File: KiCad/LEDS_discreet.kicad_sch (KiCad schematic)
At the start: 2 parts, among them U107 74HC595D,118

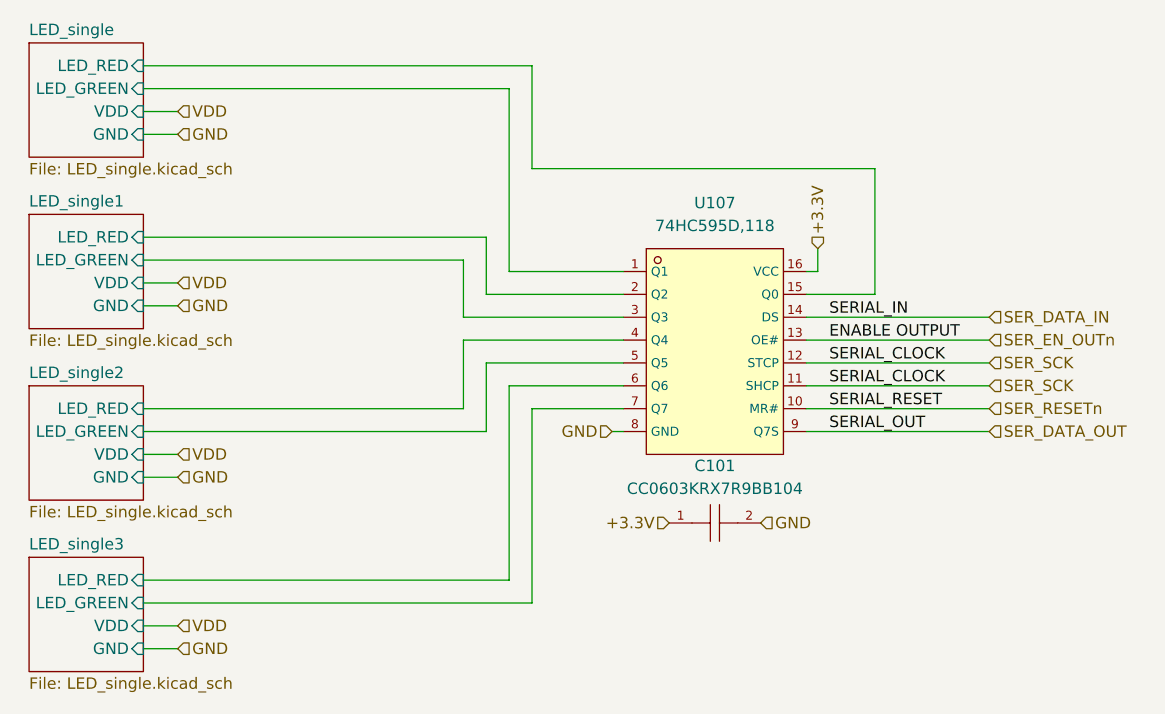
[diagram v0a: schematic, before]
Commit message: Ready for PCB layout with discreet LEDs
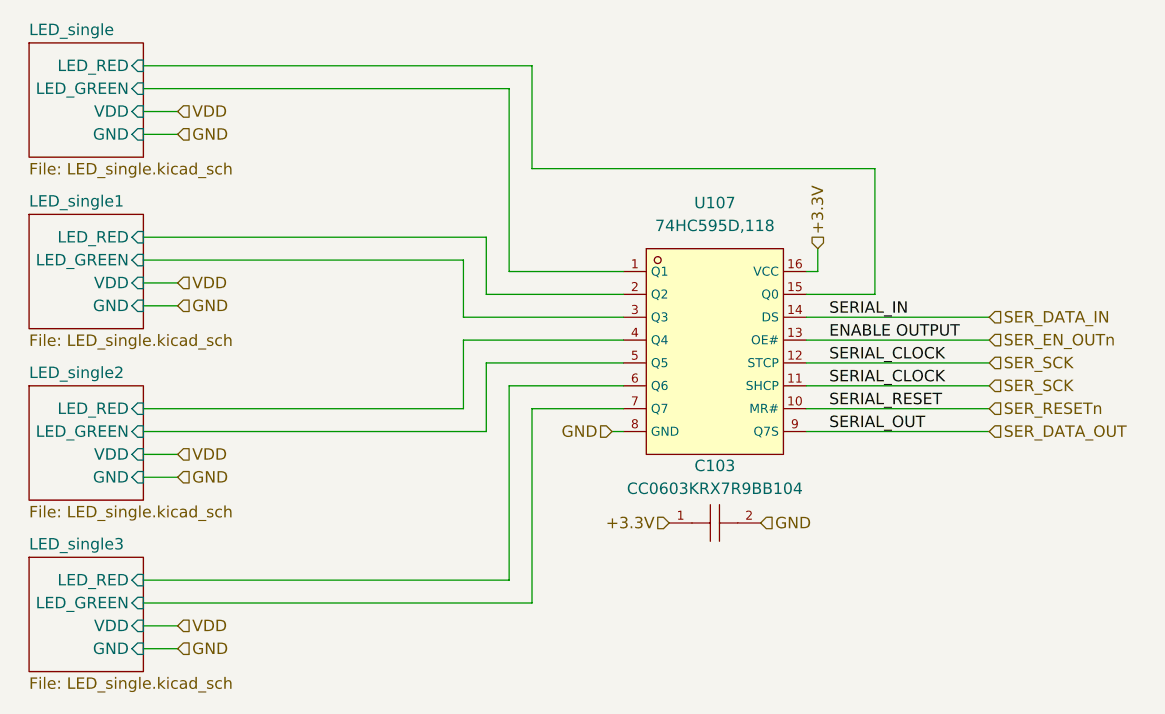
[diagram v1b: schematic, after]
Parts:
- renumbered C101 to C103
